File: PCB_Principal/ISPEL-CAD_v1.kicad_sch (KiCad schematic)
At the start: 0 parts

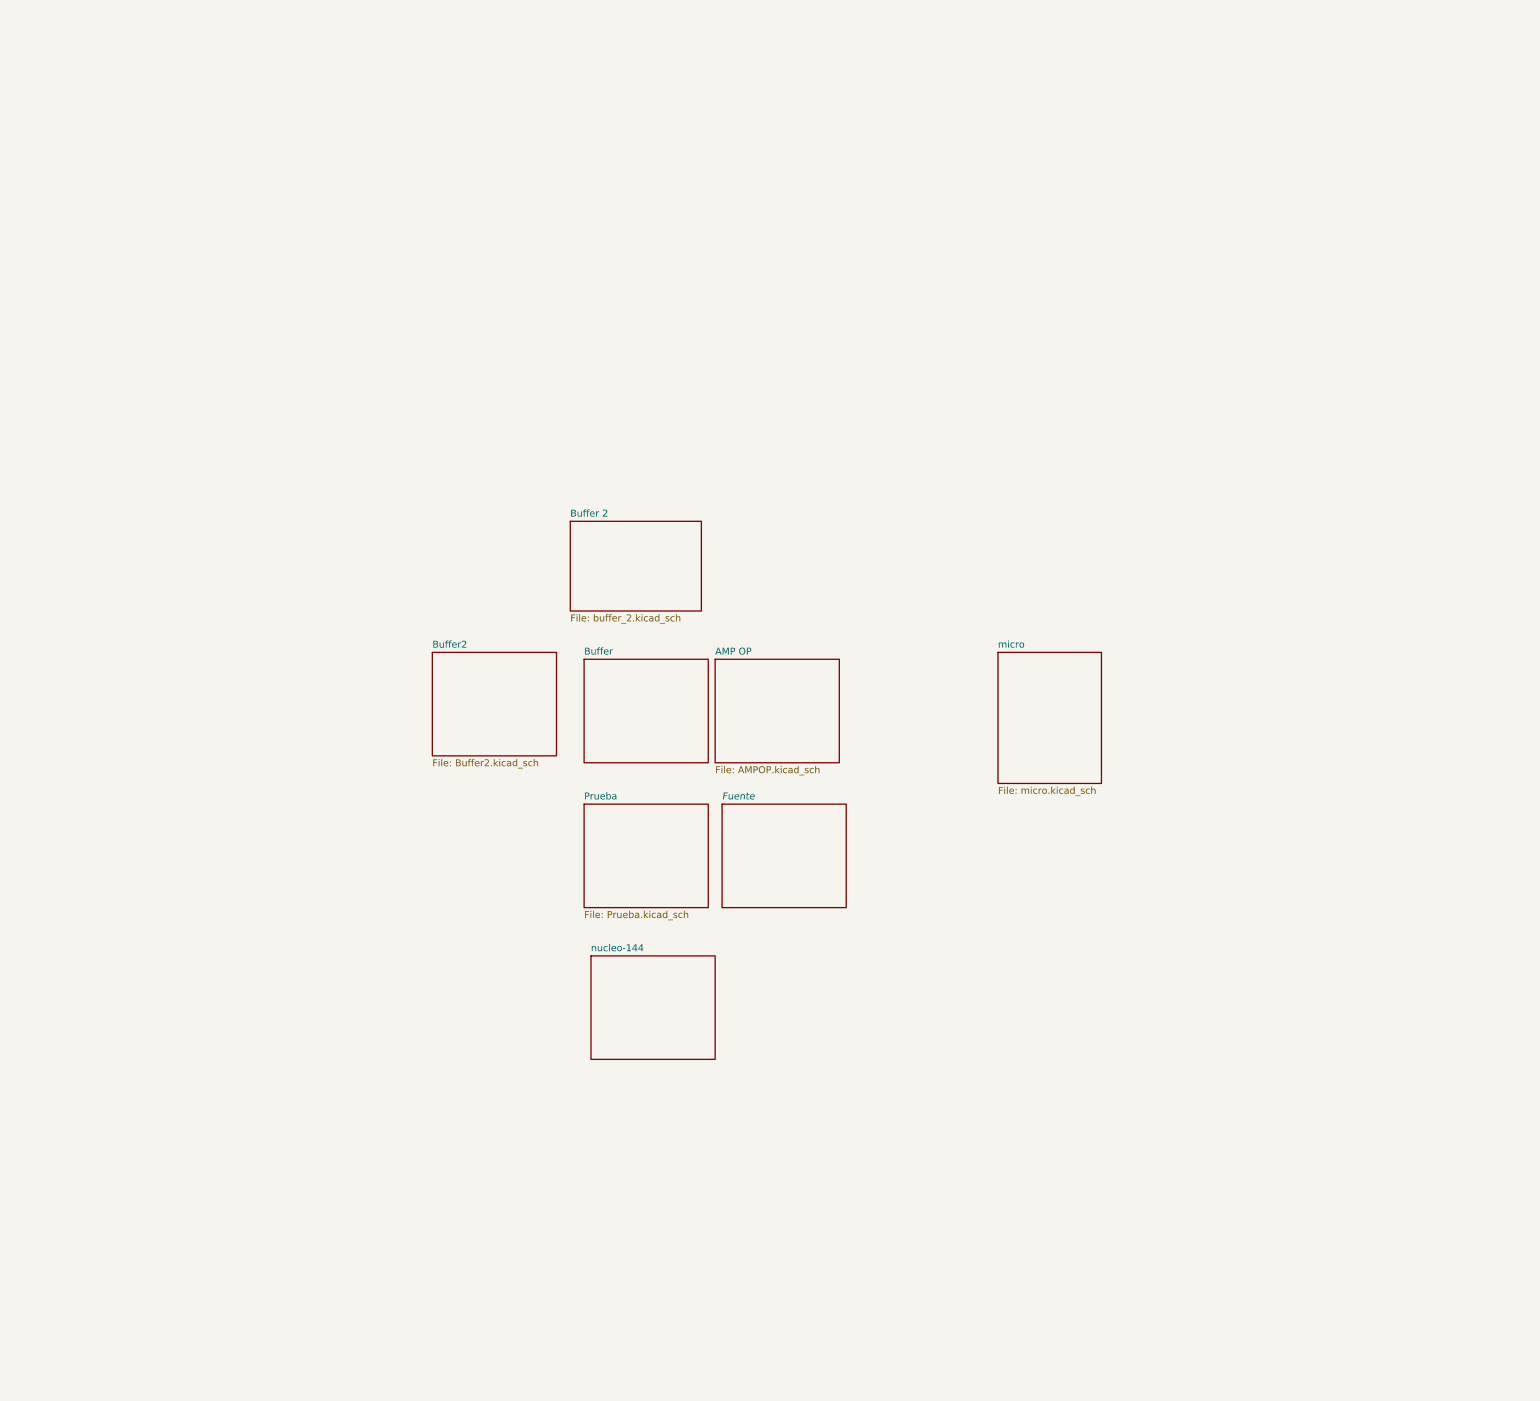
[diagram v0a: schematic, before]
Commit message: Versión 2 de esquemático, por GC.
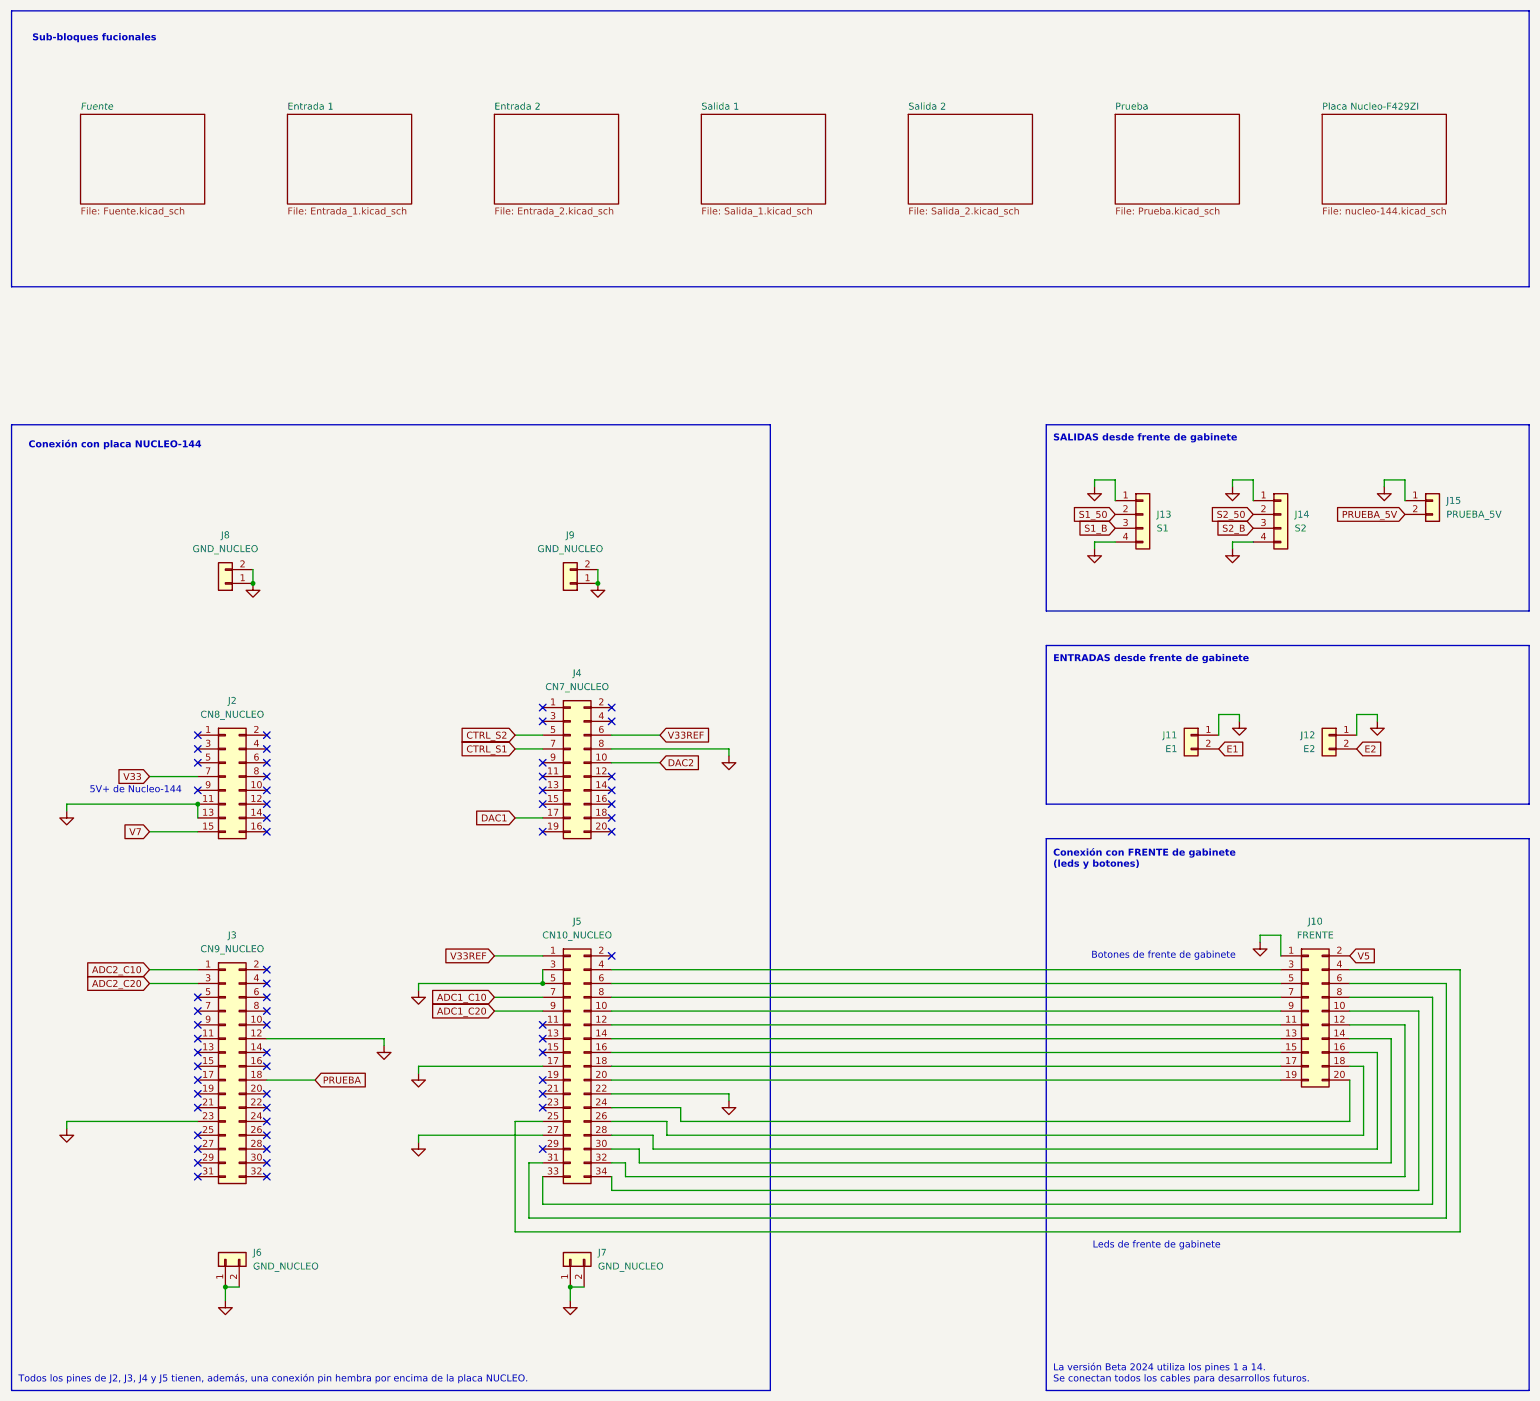
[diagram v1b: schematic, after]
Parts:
- added J10: FRENTE, Connector_IDC:IDC-Header_2x10_P2.54mm_Vertical, symbol Connector_Generic:Conn_02x10_Odd_Even
- added J11: E1, Connector_Molex:Molex_KK-254_AE-6410-02A_1x02_P2.54mm_Vertical, symbol Connector_Generic:Conn_01x02
- added J12: E2, Connector_Molex:Molex_KK-254_AE-6410-02A_1x02_P2.54mm_Vertical, symbol Connector_Generic:Conn_01x02
- added J13: S1, Connector_Molex:Molex_KK-254_AE-6410-04A_1x04_P2.54mm_Vertical, symbol Connector_Generic:Conn_01x04
- added J14: S2, Connector_Molex:Molex_KK-254_AE-6410-04A_1x04_P2.54mm_Vertical, symbol Connector_Generic:Conn_01x04
- added J15: PRUEBA_5V, Connector_Molex:Molex_KK-254_AE-6410-02A_1x02_P2.54mm_Vertical, symbol Connector_Generic:Conn_01x02
- added J2: CN8_NUCLEO, Connector_PinSocket_2.54mm:PinSocket_2x08_P2.54mm_Vertical, symbol Connector_Generic:Conn_02x08_Odd_Even
- added J3: CN9_NUCLEO, Connector_PinSocket_2.54mm:PinSocket_2x16_P2.54mm_Vertical, symbol Connector_Generic:Conn_02x16_Odd_Even
- added J4: CN7_NUCLEO, Connector_PinSocket_2.54mm:PinSocket_2x20_P2.54mm_Vertical, symbol Connector_Generic:Conn_02x10_Odd_Even
- added J5: CN10_NUCLEO, Connector_PinSocket_2.54mm:PinSocket_2x17_P2.54mm_Vertical, symbol Connector_Generic:Conn_02x17_Odd_Even
- added J6, J7, J8, J9: GND_NUCLEO, Connector_PinSocket_2.54mm:PinSocket_1x02_P2.54mm_Vertical, symbol Connector_Generic:Conn_01x02
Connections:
- new net: J10.9 (Pin_9), J5.10 (Pin_10)
- new net: J10.11 (Pin_11), J5.12 (Pin_12)
- new net: J10.13 (Pin_13), J5.14 (Pin_14)
- new net: J10.15 (Pin_15), J5.16 (Pin_16)
- new net: J10.17 (Pin_17), J5.18 (Pin_18)
- new net: J10.19 (Pin_19), J5.20 (Pin_20)
- new net: J10.20 (Pin_20), J5.24 (Pin_24)
- new net: J10.4 (Pin_4), J5.25 (Pin_25)
- new net: J10.18 (Pin_18), J5.26 (Pin_26)
- new net: J10.16 (Pin_16), J5.28 (Pin_28)
- new net: J10.14 (Pin_14), J5.30 (Pin_30)
- new net: J10.6 (Pin_6), J5.31 (Pin_31)
- new net: J10.12 (Pin_12), J5.32 (Pin_32)
- new net: J10.8 (Pin_8), J5.33 (Pin_33)
- new net: J10.10 (Pin_10), J5.34 (Pin_34)
- new net: J10.3 (Pin_3), J5.4 (Pin_4)
- new net: J10.5 (Pin_5), J5.6 (Pin_6)
- new net: J10.7 (Pin_7), J5.8 (Pin_8)
- new net ADC1_C10: J5.7 (Pin_7)
- new net ADC1_C20: J5.9 (Pin_9)
- new net ADC2_C10: J3.1 (Pin_1)
- new net ADC2_C20: J3.3 (Pin_3)
- new net CTRL_S1: J4.7 (Pin_7)
- new net CTRL_S2: J4.5 (Pin_5)
- new net DAC1: J4.17 (Pin_17)
- new net DAC2: J4.10 (Pin_10)
- new net E1: J11.2 (Pin_2)
- new net E2: J12.2 (Pin_2)
- new net GND: J10.1 (Pin_1), J11.1 (Pin_1), J12.1 (Pin_1), J13.1 (Pin_1), J13.4 (Pin_4), J14.1 (Pin_1), J14.4 (Pin_4), J15.1 (Pin_1), J2.11 (Pin_11), J2.13 (Pin_13), J3.12 (Pin_12), J3.23 (Pin_23), J4.8 (Pin_8), J5.17 (Pin_17), J5.22 (Pin_22), J5.27 (Pin_27), J5.3 (Pin_3), J5.5 (Pin_5), J6.1 (Pin_1), J6.2 (Pin_2), J7.1 (Pin_1), J7.2 (Pin_2), J8.1 (Pin_1), J8.2 (Pin_2), J9.1 (Pin_1), J9.2 (Pin_2)
- new net PRUEBA: J3.18 (Pin_18)
- new net PRUEBA_5V: J15.2 (Pin_2)
- new net S1_50: J13.2 (Pin_2)
- new net S1_B: J13.3 (Pin_3)
- new net S2_50: J14.2 (Pin_2)
- new net S2_B: J14.3 (Pin_3)
- new net V33: J2.7 (Pin_7)
- new net V33REF: J4.6 (Pin_6), J5.1 (Pin_1)
- new net V5: J10.2 (Pin_2)
- new net V7: J2.15 (Pin_15)
- no-connect marks 0 -> 61
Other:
- sheet Buffer 2 renamed Entrada 1
- sheet micro renamed Placa Nucleo-F429ZI
- removed sheet AMP OP
- removed sheet Buffer
- removed sheet Buffer2
- removed sheet nucleo-144
- added sheet Entrada 2 (Entrada_2.kicad_sch)
- added sheet Salida 1 (Salida_1.kicad_sch)
- added sheet Salida 2 (Salida_2.kicad_sch)
- sheet Entrada 1: file buffer_2.kicad_sch -> Entrada_1.kicad_sch
- sheet Placa Nucleo-F429ZI: file micro.kicad_sch -> nucleo-144.kicad_sch
- note added: "5V+ de Nucleo-144"
- note added: "Botones de frente de gabinete"
- note added: "Conexión con FRENTE de gabinete (leds y botones)"
- note added: "Conexión con placa NUCLEO-144"
- note added: "ENTRADAS desde frente de gabinete"
- note added: "La versión Beta 2024 utiliza los pines 1 a 14. Se conectan todos los cables para desarrollos futuros."
- note added: "Leds de frente de gabinete"
- note added: "SALIDAS desde frente de gabinete"
- note added: "Sub-bloques fucionales"
- note added: "Todos los pines de J2, J3, J4 y J5 tienen, además, una conexión pin hembra por encima de la placa NUCLEO."
- company: (none) -> Undav
- title: (none) -> Placa principal ISPEL Beta 2024

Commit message: Iniciando PCB...
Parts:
- added FID1, FID2: Fiducial, Fiducial:Fiducial_1mm_Mask3mm, symbol Mechanical:Fiducial
- added H1, H2, H3, H4: MountingHole, MountingHole:MountingHole_3.2mm_M3, symbol Mechanical:MountingHole
- added J1: Vin, TerminalBlock_Phoenix:TerminalBlock_Phoenix_MKDS-1,5-3-5.08_1x03_P5.08mm_Horizontal, symbol Connector:Screw_Terminal_01x03
- J7: renamed from J4; footprint Connector_PinSocket_2.54mm:PinSocket_2x20_P2.54mm_Vertical -> Connector_PinSocket_2.54mm:PinSocket_2x10_P2.54mm_Vertical
- renumbered J11 to J10, J13 to J11, J14 to J13, J10 to J14, J8 to J2, J2 to J3, J3 to J4, J6 to J5, J9 to J6, J5 to J8, J7 to J9
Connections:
- net GND: now also J1.2 (Pin_2)
- new net VAC1: J1.3 (Pin_3)
- new net VAC2: J1.1 (Pin_1)
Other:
- note added: "0V"
- note added: "Entrada de alimentación"
- note added: "VAC1"
- note added: "VAC2"
- moved on the sheet: J10, J11, J12, J13, J14, J15, J2, J3, J4, J5, J6, J7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

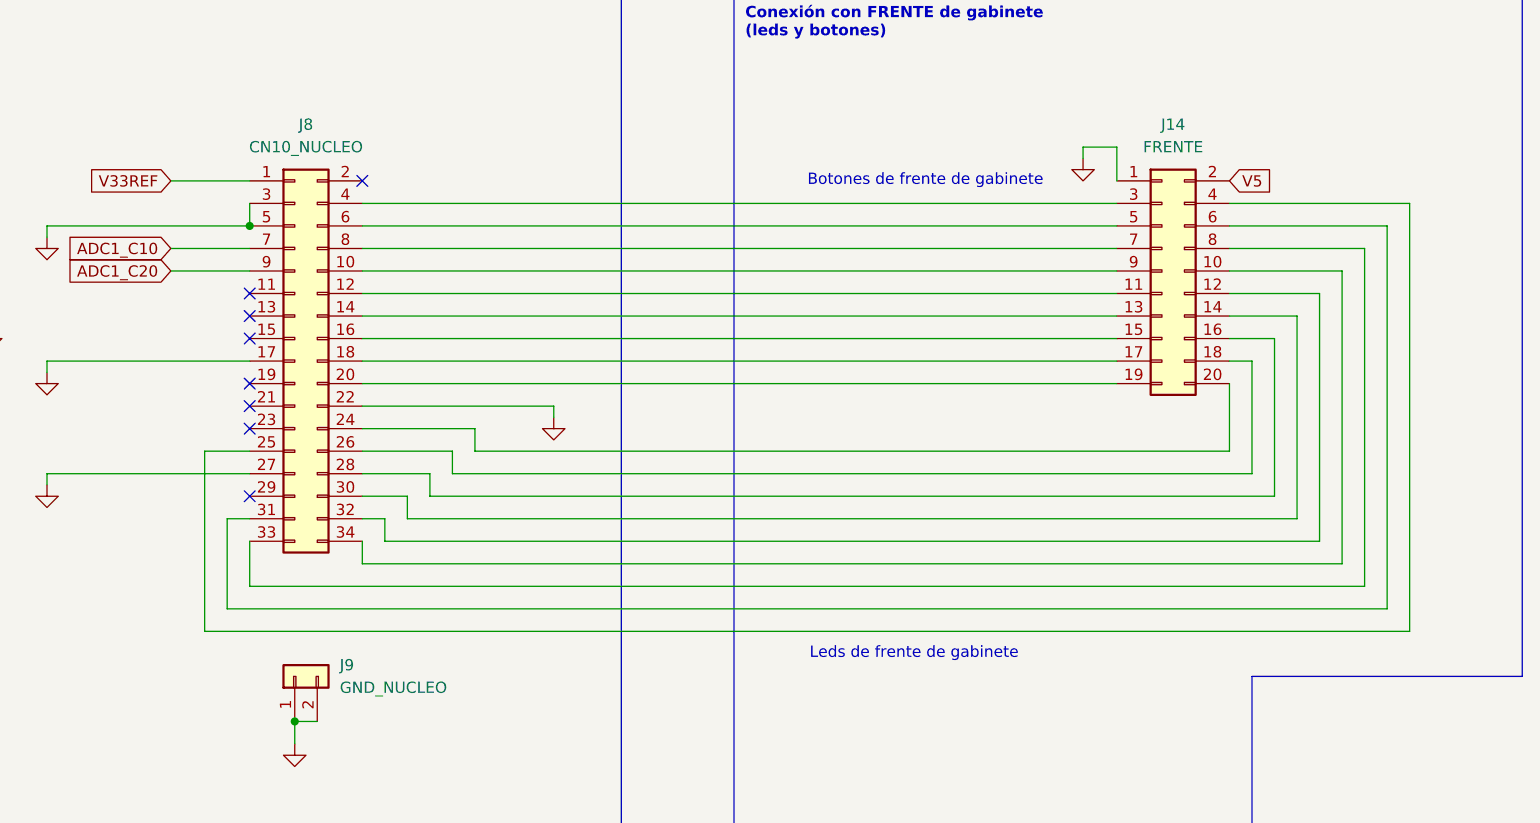
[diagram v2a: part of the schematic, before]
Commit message: Placa con conector J8.
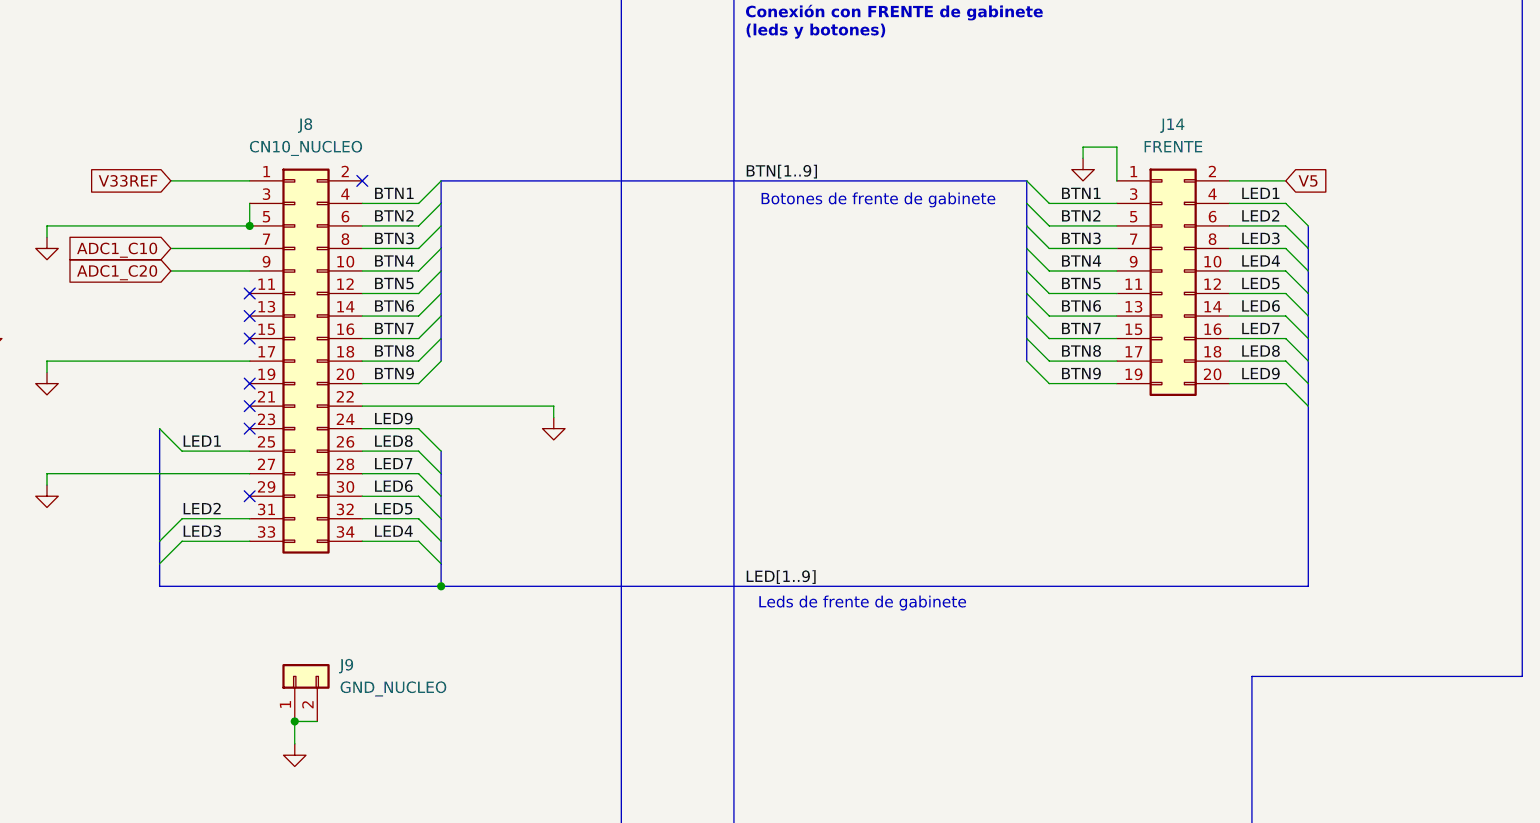
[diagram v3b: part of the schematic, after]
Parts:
- J8: footprint Connector_PinSocket_2.54mm:PinSocket_2x17_P2.54mm_Vertical -> Libreria_ISPEL:PinSocket_2x17_P2.54mm_Vertical_impar-par
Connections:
- net BTN4: now reaches J14.9 (Pin_9), J8.10 (Pin_10)
- net BTN5: now reaches J14.11 (Pin_11), J8.12 (Pin_12)
- net BTN6: now reaches J14.13 (Pin_13), J8.14 (Pin_14)
- net BTN7: now reaches J14.15 (Pin_15), J8.16 (Pin_16)
- net BTN8: now reaches J14.17 (Pin_17), J8.18 (Pin_18)
- net BTN9: now reaches J14.19 (Pin_19), J8.20 (Pin_20)
- net LED9: now reaches J14.20 (Pin_20), J8.24 (Pin_24)
- net LED1: now reaches J14.4 (Pin_4), J8.25 (Pin_25)
- net LED8: now reaches J14.18 (Pin_18), J8.26 (Pin_26)
- net LED7: now reaches J14.16 (Pin_16), J8.28 (Pin_28)
- net LED6: now reaches J14.14 (Pin_14), J8.30 (Pin_30)
- net LED2: now reaches J14.6 (Pin_6), J8.31 (Pin_31)
- net LED5: now reaches J14.12 (Pin_12), J8.32 (Pin_32)
- net LED3: now reaches J14.8 (Pin_8), J8.33 (Pin_33)
- net LED4: now reaches J14.10 (Pin_10), J8.34 (Pin_34)
- net BTN1: now reaches J14.3 (Pin_3), J8.4 (Pin_4)
- net BTN2: now reaches J14.5 (Pin_5), J8.6 (Pin_6)
- net BTN3: now reaches J14.7 (Pin_7), J8.8 (Pin_8)
